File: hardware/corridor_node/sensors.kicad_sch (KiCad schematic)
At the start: 14 parts, among them J1 RDB223, U4 LMV321, U4 TTY020-CA6

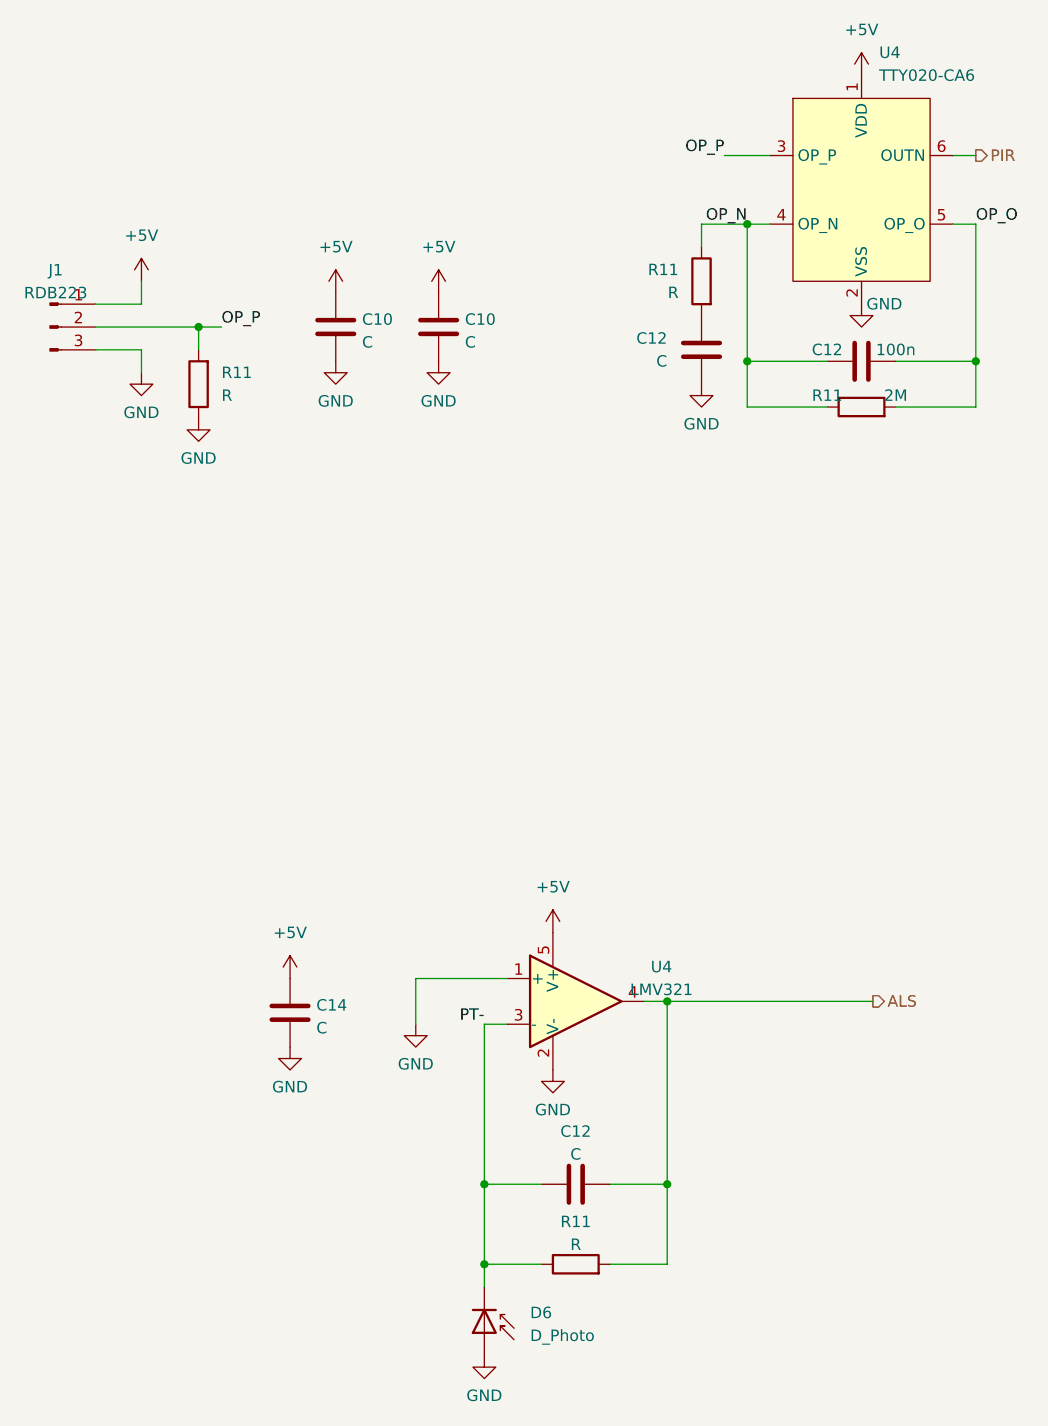
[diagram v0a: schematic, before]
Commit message: led balance and corridor ready
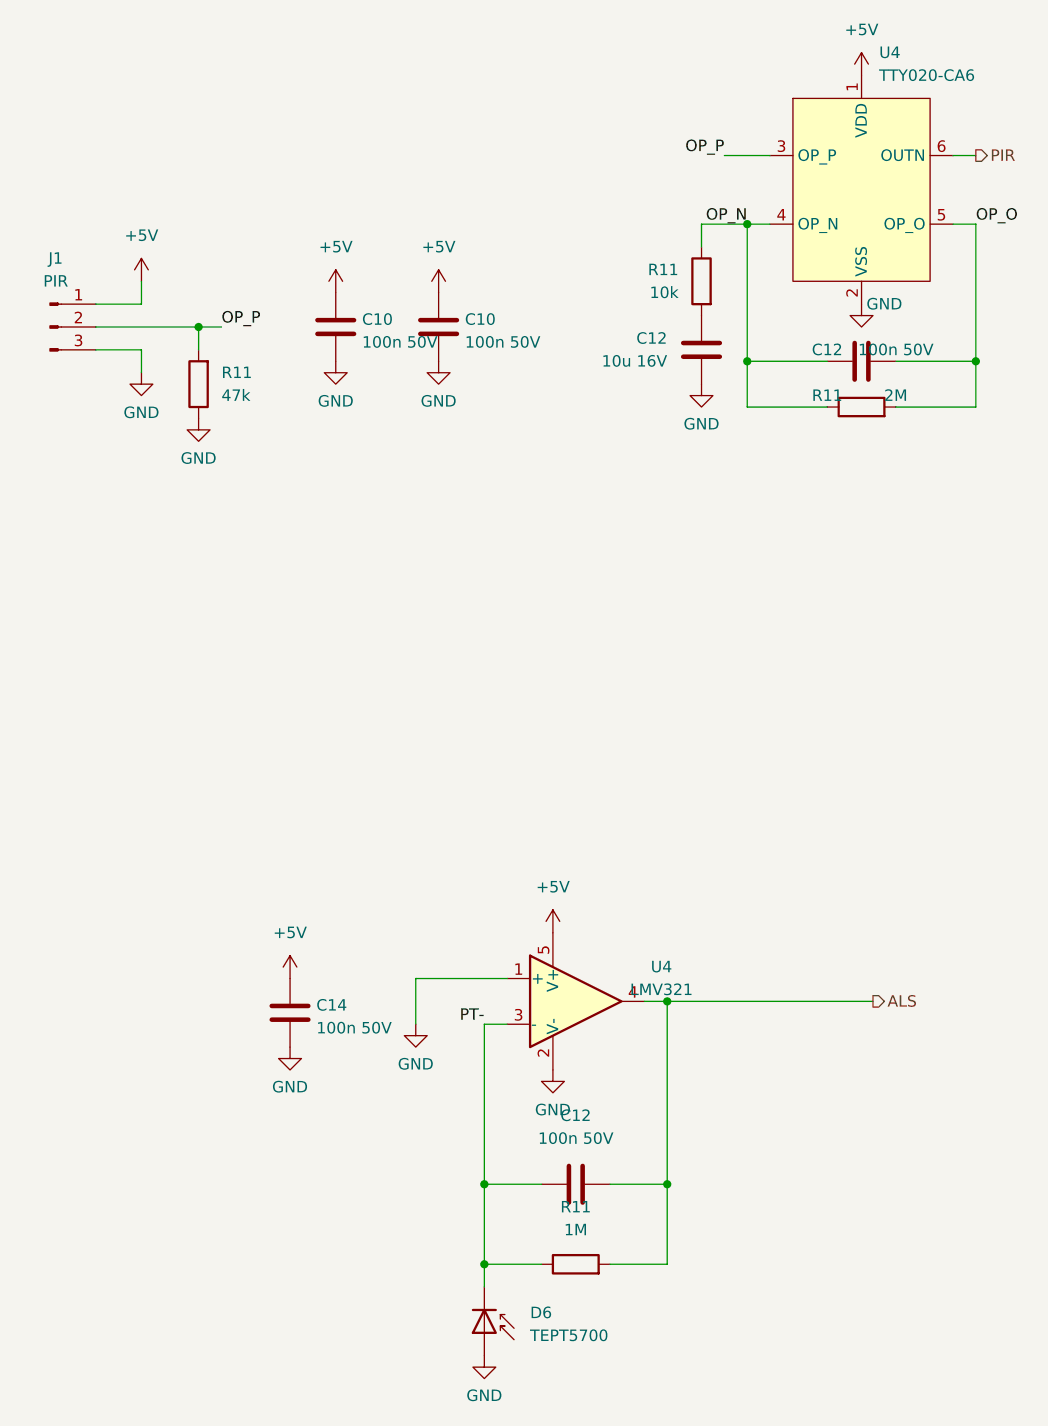
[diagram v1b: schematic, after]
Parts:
- C10, C12, C14: value C -> 100n 50V; LCSC Part # (none) -> C14663
- C12: value C -> 10u 16V; LCSC Part # (none) -> C92487
- C12: value 100n -> 100n 50V; LCSC Part # (none) -> C14663
- D6: value D_Photo -> TEPT5700; LCSC Part # (none) -> C141763
- J1: value RDB223 -> PIR; LCSC Part # (none) -> C6081342
- R11: value R -> 47k; LCSC Part # (none) -> C105579
- R11: value R -> 10k; LCSC Part # (none) -> C98220
- R11: LCSC Part # (none) -> C114615
- R11: value R -> 1M; LCSC Part # (none) -> C105578
- U4: LCSC Part # (none) -> C7972
- U4: LCSC Part # (none) -> C648790
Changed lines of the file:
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@@
       (effects (font (size 1.27 1.27)) (justify right))
     )
-    (property "Value" "C" (at 127 58.42 0)
+    (property "Value" "10u 16V" (at 127 58.42 0)
       (effects (font (size 1.27 1.27)) (justify right))
     )
@@
     )
     (property "Datasheet" "~" (at 130.81 57.15 0)
+      (effects (font (size 1.27 1.27)) hide)
+    )
+    (property "LCSC Part #" "C92487" (at 130.81 57.15 0)
       (effects (font (size 1.27 1.27)) hide)
     )
@@
       (effects (font (size 1.27 1.27)) (justify right))
     )
-    (property "Value" "R" (at 77.47 62.23 0)
+    (property "Value" "47k" (at 77.47 62.23 0)
       (effects (font (size 1.27 1.27)) (justify right))
     )
@@
       (effects (font (size 1.27 1.27)) hide)
     )
+    (property "LCSC Part #" "C105579" (at 74.93 60.96 0)
+      (effects (font (size 1.27 1.27)) hide)
+    )
     (pin "1")
     (pin "2")
@@
       (effects (font (size 1.27 1.27)) (justify left))
     )
-    (property "Value" "R" (at 128.27 50.8 0)
+    (property "Value" "10k" (at 128.27 50.8 0)
       (effects (font (size 1.27 1.27)) (justify left))
     )
@@
       (effects (font (size 1.27 1.27)) hide)
     )
+    (property "LCSC Part #" "C98220" (at 130.81 49.53 0)
+      (effects (font (size 1.27 1.27)) hide)
+    )
     (pin "1")
     (pin "2")
@@
   (symbol (lib_id "Connector:Conn_01x03_Male") (at 58.42 54.61 0) (unit 1)
     (in_bom yes) (on_board yes) (dnp no) (fields_autoplaced)
-    (property "Reference" "J1" (at 59.055 48.294 0)
-      (effects (font (size 1.27 1.27)))
-    )
-    (property "Value" "RDB223" (at 59.055 50.8309 0)
+    (property "Reference" "J1" (at 59.055 46.99 0)
+      (effects (font (size 1.27 1.27)))
+    )
+    (property "Value" "PIR" (at 59.055 49.53 0)
       (effects (font (size 1.27 1.27)))
     )
@@
       (effects (font (size 1.27 1.27)) hide)
     )
-    (property "Datasheet" "~" (at 58.42 54.61 0)
+    (property "Datasheet" "https://datasheet.lcsc.com/lcsc/2305231101_NEWOPTO-XYC-PIR203Z-S0_C6081342.pdf" (at 58.42 54.61 0)
+      (effects (font (size 1.27 1.27)) hide)
+    )
+    (property "LCSC Part #" "C6081342" (at 58.42 54.61 0)
       (effects (font (size 1.27 1.27)) hide)
     )
@@
       (project "corridor_node"
         (path "/d4c2f312-ca5d-462b-a371-0fb5d5a0cf93/9cf16ded-83b6-47fc-84db-022e02199eee"
-          (reference "J3") (unit 1)
+          (reference "U6") (unit 1)
         )
       )
@@
       (effects (font (size 1.27 1.27)) (justify left))
     )
-    (property "Value" "C" (at 88.011 132.5122 0)
+    (property "Value" "100n 50V" (at 88.011 132.5122 0)
       (effects (font (size 1.27 1.27)) (justify left))
     )
@@
     )
     (property "Datasheet" "~" (at 85.09 130.81 0)
+      (effects (font (size 1.27 1.27)) hide)
+    )
+    (property "LCSC Part #" "C14663" (at 85.09 130.81 0)
       (effects (font (size 1.27 1.27)) hide)
     )
@@
     )
     (property "Datasheet" "http://www.ti.com/lit/ds/symlink/lmv324.pdf" (at 116.84 129.54 0)
+      (effects (font (size 1.27 1.27)) hide)
+    )
+    (property "LCSC Part #" "C7972" (at 116.84 129.54 0)
       (effects (font (size 1.27 1.27)) hide)
     )
@@
       (effects (font (size 1.27 1.27)) hide)
     )
+    (property "LCSC Part #" "C114615" (at 148.59 63.5 0)
+      (effects (font (size 1.27 1.27)) hide)
+    )
     (pin "1")
     (pin "2")
@@
       (effects (font (size 1.27 1.27)))
     )
-    (property "Value" "100n" (at 152.4 57.15 90)
+    (property "Value" "100n 50V" (at 152.4 57.15 90)
       (effects (font (size 1.27 1.27)))
     )
@@
       (effects (font (size 1.27 1.27)) hide)
     )
+    (property "LCSC Part #" "C14663" (at 148.59 58.42 0)
+      (effects (font (size 1.27 1.27)) hide)
+    )
     (pin "1")
     (pin "2")
@@
     )
     (property "Datasheet" "https://www.tontek.com.tw/uploads/product/166/TTY020_V1.3_EN%20.pdf" (at 148.59 39.37 0)
+      (effects (font (size 1.27 1.27)) hide)
+    )
+    (property "LCSC Part #" "C648790" (at 148.59 39.37 0)
       (effects (font (size 1.27 1.27)) hide)
     )
@@
       (effects (font (size 1.27 1.27)) (justify left))
     )
-    (property "Value" "C" (at 93.091 56.3122 0)
+    (property "Value" "100n 50V" (at 93.091 56.3122 0)
       (effects (font (size 1.27 1.27)) (justify left))
     )
@@
     )
     (property "Datasheet" "~" (at 90.17 54.61 0)
+      (effects (font (size 1.27 1.27)) hide)
+    )
+    (property "LCSC Part #" "C14663" (at 90.17 54.61 0)
       (effects (font (size 1.27 1.27)) hide)
     )
@@
       (effects (font (size 1.27 1.27)) (justify left))
     )
-    (property "Value" "C" (at 104.521 56.3122 0)
+    (property "Value" "100n 50V" (at 104.521 56.3122 0)
       (effects (font (size 1.27 1.27)) (justify left))
     )
@@
       (effects (font (size 1.27 1.27)) hide)
     )
+    (property "LCSC Part #" "C14663" (at 101.6 54.61 0)
+      (effects (font (size 1.27 1.27)) hide)
+    )
     (pin "1")
     (pin "2")
@@
       (effects (font (size 1.27 1.27)) (justify left))
     )
-    (property "Value" "D_Photo" (at 111.76 166.6875 90)
+    (property "Value" "TEPT5700" (at 111.76 166.6875 90)
       (effects (font (size 1.27 1.27)) (justify left))
     )
@@
       (effects (font (size 1.27 1.27)) hide)
     )
+    (property "LCSC Part #" "C141763" (at 106.68 166.37 0)
+      (effects (font (size 1.27 1.27)) hide)
+    )
     (pin "1")
     (pin "2")
@@
   (symbol (lib_id "Device:R") (at 116.84 158.75 90) (unit 1)
     (in_bom yes) (on_board yes) (dnp no) (fields_autoplaced)
-    (property "Reference" "R11" (at 116.84 154.0342 90)
-      (effects (font (size 1.27 1.27)))
-    )
-    (property "Value" "R" (at 116.84 156.5711 90)
+    (property "Reference" "R11" (at 116.84 152.4 90)
+      (effects (font (size 1.27 1.27)))
+    )
+    (property "Value" "1M" (at 116.84 154.94 90)
       (effects (font (size 1.27 1.27)))
     )
@@
       (effects (font (size 1.27 1.27)) hide)
     )
+    (property "LCSC Part #" "C105578" (at 116.84 158.75 0)
+      (effects (font (size 1.27 1.27)) hide)
+    )
     (pin "1")
     (pin "2")
@@
   (symbol (lib_id "Device:C") (at 116.84 149.86 90) (unit 1)
     (in_bom yes) (on_board yes) (dnp no) (fields_autoplaced)
-    (property "Reference" "C12" (at 116.84 144.0012 90)
-      (effects (font (size 1.27 1.27)))
-    )
-    (property "Value" "C" (at 116.84 146.5381 90)
+    (property "Reference" "C12" (at 116.84 142.24 90)
+      (effects (font (size 1.27 1.27)))
+    )
+    (property "Value" "100n 50V" (at 116.84 144.78 90)
       (effects (font (size 1.27 1.27)))
     )
@@
       (effects (font (size 1.27 1.27)) hide)
     )
+    (property "LCSC Part #" "C14663" (at 116.84 149.86 0)
+      (effects (font (size 1.27 1.27)) hide)
+    )

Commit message: various
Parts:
- D6: value TEPT5700 -> SFH203; LCSC Part # C141763 -> (none)
- R11: value 1M -> 10M
- U4: value LMV321 -> MCP6231UT; LCSC Part # C7972 -> (none)
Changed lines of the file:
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@@
       (effects (font (size 1.27 1.27)))
     )
-    (property "Value" "LMV321" (at 126.3597 128.2502 0)
+    (property "Value" "MCP6231UT" (at 126.3597 128.2502 0)
       (effects (font (size 1.27 1.27)))
     )
@@
       (effects (font (size 1.27 1.27)) hide)
     )
-    (property "LCSC Part #" "C7972" (at 116.84 129.54 0)
+    (property "LCSC Part #" "" (at 116.84 129.54 0)
       (effects (font (size 1.27 1.27)) hide)
     )
@@
       (effects (font (size 1.27 1.27)) (justify left))
     )
-    (property "Value" "TEPT5700" (at 111.76 166.6875 90)
+    (property "Value" "SFH203" (at 111.76 166.6875 90)
       (effects (font (size 1.27 1.27)) (justify left))
     )
@@
       (effects (font (size 1.27 1.27)) hide)
     )
-    (property "LCSC Part #" "C141763" (at 106.68 166.37 0)
+    (property "LCSC Part #" "" (at 106.68 166.37 0)
       (effects (font (size 1.27 1.27)) hide)
     )
@@
       (effects (font (size 1.27 1.27)))
     )
-    (property "Value" "1M" (at 116.84 154.94 90)
-      (effects (font (size 1.27 1.27)))
-    )
+    (property "Value" "10M" (at 116.84 154.94 90)
+      (effects (font (size 1.27 1.27)))
+    )

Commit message: nightLight pcb files version upgrade
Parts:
- renumbered C14 to C10, C12 to C11, C10 to C15, C12 to C7, C10 to C8, C12 to C9, R11 to R10, R11 to R5, R11 to R8, R11 to R9, U4 to U3, J1 to U6
